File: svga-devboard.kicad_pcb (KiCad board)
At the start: 4 copper layers, 130 x 106.7 mm, 40 parts, among them J1 Bus_PCI_32bit_Universal, U1 SN74LVCH16T245DGGR, U2 SN74LVCH16T245DGGR, U3 SN74LVCH16T245DGGR, U4 SN74LVCH16T245DGGR, U5 SN74LVCH16T245DGGR

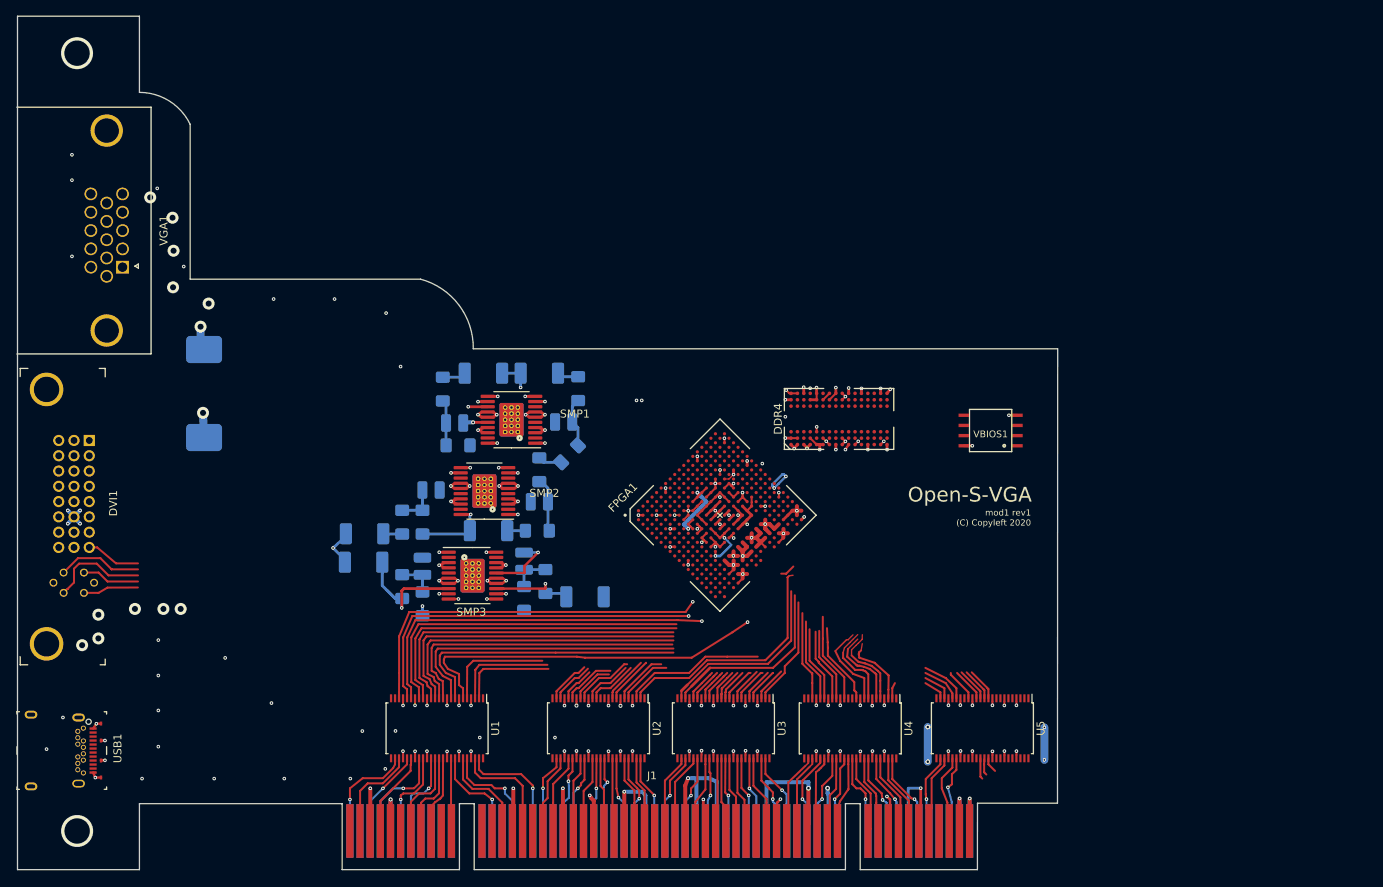
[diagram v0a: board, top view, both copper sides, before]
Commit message: Add files via upload
Converted to hierarchical scheets, added support-components for SMPS-units - many other changes.
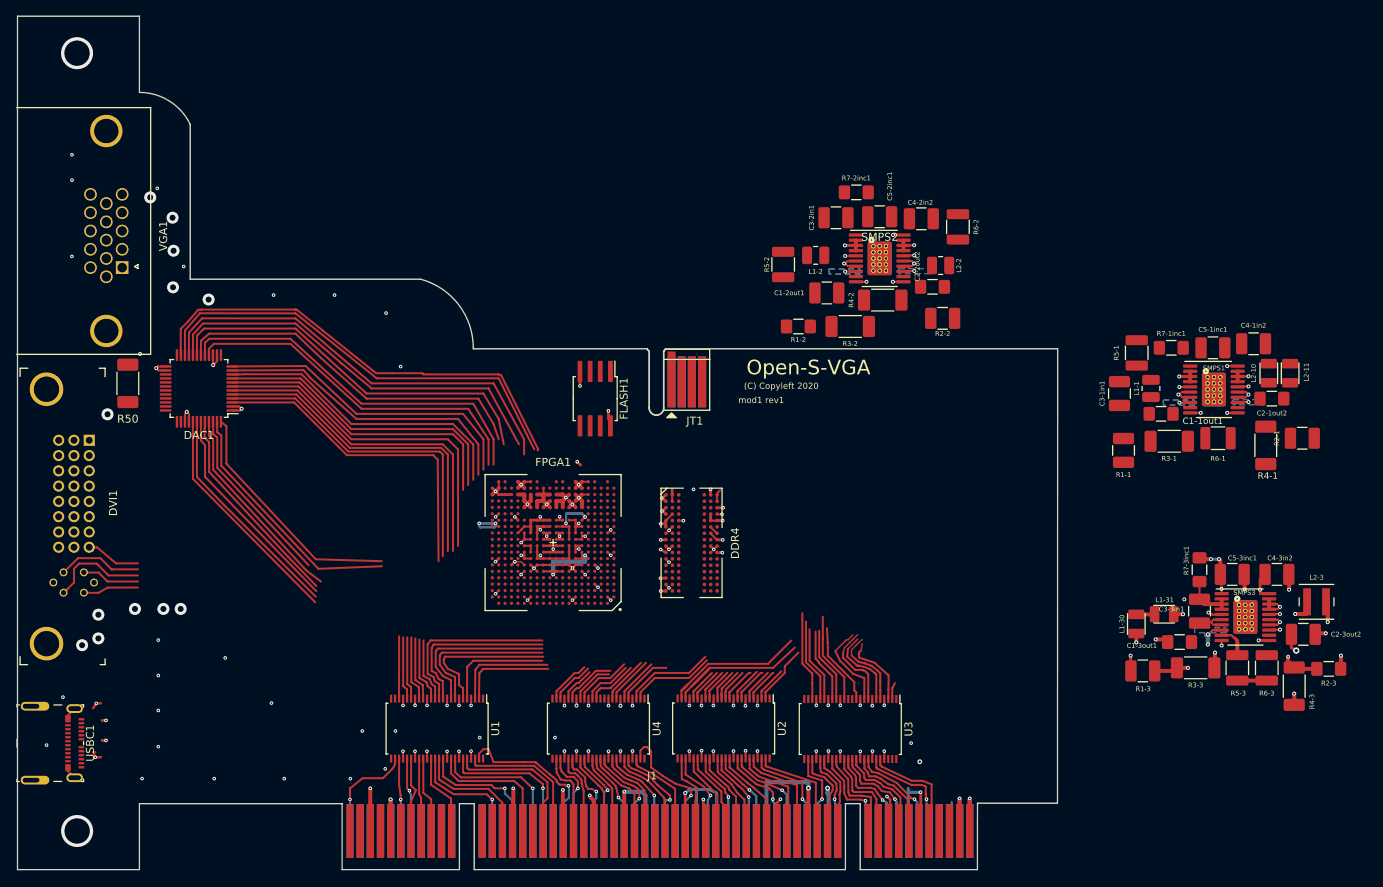
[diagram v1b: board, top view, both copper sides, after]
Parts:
- removed C1-1, C1-2, C1-3, C2-1, C2-2, C2-3: 22UF-1206-16V-10%, Capacitor_SMD:C_1206_3216Metric_Pad1.42x1.75mm_HandSolder
- removed L1-3, L2-1: 1008PS-102KLC, Inductor_SMD:L_1008_2520Metric
- removed SMP1, SMP2, SMP3: LM26420-Q1MHX_NOPB, Package_SO:HTSSOP-20-1EP_4.4x6.5mm_P0.42mm_EP3.2x6.4mm_Mask3.0x4.2mm_ThermalVias
- removed U5: SN74LVCH16T245DGGR, Package_SO:TSSOP-48_6.1x12.5mm_P0.5mm
- removed USB1: USB_C_Amphenol_10133476-10001LF, Connector_USB:USB-C_Female_10133476-10001LF
- removed VBIOS1: Cypress_Semi_S25FL128LAGMFV013, Package_SO:Cypress_Semi_S25FL128LAGMFV013
- added C1-1out1: C3216X7S0J336M160AC, Capacitor_SMD:C_1206_3216Metric_Pad1.42x1.75mm_HandSolder, F.Cu at (221.9, 76.8)
- added C1-2out1: C3225X7R1C226M250AC, Capacitor_SMD:C_1210_3225Metric_Pad1.42x2.65mm_HandSolder, F.Cu at (180.1, 61.7)
- added C1-3out1: C3216X7S0J336M160AC, Capacitor_SMD:C_1206_3216Metric_Pad1.42x1.75mm_HandSolder, F.Cu at (224.2, 105.4)
- added C2-1out2: C3216X7S0J336M160AC, Capacitor_SMD:C_1206_3216Metric_Pad1.42x1.75mm_HandSolder, F.Cu at (235.7, 74.9)
- added C2-2out2: C3216X7S0J336M160AC, Capacitor_SMD:C_1206_3216Metric_Pad1.42x1.75mm_HandSolder, F.Cu at (193.3, 61.0)
- added C2-3out2: C3225X7R1C226M250AC, Capacitor_SMD:C_1210_3225Metric_Pad1.42x2.65mm_HandSolder, F.Cu at (239.6, 104.4)
- added C3-1in1: C1210C156K8PACTU, Capacitor_SMD:C_1210_3225Metric_Pad1.42x2.65mm_HandSolder, F.Cu at (216.7, 74.3)
- added C3-2in1: C1210C156K8PACTU, Capacitor_SMD:C_1210_3225Metric_Pad1.42x2.65mm_HandSolder, F.Cu at (181.2, 52.3)
- added C3-3in1: C1210C156K8PACTU, Capacitor_SMD:C_1210_3225Metric_Pad1.42x2.65mm_HandSolder, F.Cu at (226.7, 101.5)
- added C4-1in2: C1210C156K8PACTU, Capacitor_SMD:C_1210_3225Metric_Pad1.42x2.65mm_HandSolder, F.Cu at (233.4, 68.1)
- added C4-2in2: C1210C156K8PACTU, Capacitor_SMD:C_1210_3225Metric_Pad1.42x2.65mm_HandSolder, F.Cu at (191.9, 52.5)
- added C4-3in2: C1210C156K8PACTU, Capacitor_SMD:C_1210_3225Metric_Pad1.42x2.65mm_HandSolder, F.Cu at (236.3, 96.9)
- added C5-1inc1: C1210C474K5RACTU, Capacitor_SMD:C_1210_3225Metric_Pad1.42x2.65mm_HandSolder, F.Cu at (228.3, 68.6)
- added C5-2inc1: C1210C474K5RACTU, Capacitor_SMD:C_1210_3225Metric_Pad1.42x2.65mm_HandSolder, F.Cu at (186.7, 52.2)
- added C5-3inc1: C1210C474K5RACTU, Capacitor_SMD:C_1210_3225Metric_Pad1.42x2.65mm_HandSolder, F.Cu at (230.8, 96.9)
- added DAC1: ADV7125KSTZ50, Package_QFP:LQFP-48_7x7mm_P0.5mm, F.Cu at (101.6, 73.7)
- added FLASH1: ISSI_IS25LP128F-JBLE, Package_SO:SOIC-8_5.28x5.28mm_P1.27mm, F.Cu at (151.1, 74.9)
- added JT1: JT1, Connector_PCBEdge:con-pcb-slot-CONN_SLOT, F.Cu at (162.6, 72.6)
- added L1-30: MAKK2520HR22M, Inductor_SMD:L_Taiyo-Yuden_MA-2520_HandSoldering, F.Cu at (218.8, 103.1)
- added L1-31: MAKK2520HR33M, Inductor_SMD:L_Taiyo-Yuden_MA-2520_HandSoldering, F.Cu at (222.2, 101.9)
- added L2-10: MAKK2520HR22M, Inductor_SMD:L_Taiyo-Yuden_MA-2520_HandSoldering, F.Cu at (235.3, 71.8)
- added L2-11: MAKK2520HR33M, Inductor_SMD:L_Taiyo-Yuden_MA-2520_HandSoldering, F.Cu at (238.0, 71.8)
- added R5-1: RC1210FR-0749K9L, Resistor_SMD:R_YAGEO_1210_3225Metric_HandSolder, F.Cu at (218.8, 69.2)
- added R5-2: RC1210FR-0749K9L, Resistor_SMD:R_YAGEO_1210_3225Metric_HandSolder, F.Cu at (174.6, 58.2)
- added R5-3: RC1210FR-0749K9L, Resistor_SMD:R_YAGEO_1210_3225Metric_HandSolder, F.Cu at (231.4, 108.6)
- added R6-1: RC1210FR-0749K9L, Resistor_SMD:R_YAGEO_1210_3225Metric_HandSolder, F.Cu at (229.0, 79.9)
- added R6-2: RC1210FR-0749K9L, Resistor_SMD:R_YAGEO_1210_3225Metric_HandSolder, F.Cu at (196.5, 53.5)
- added R6-3: RC1210FR-0749K9L, Resistor_SMD:R_YAGEO_1210_3225Metric_HandSolder, F.Cu at (235.1, 108.6)
- added R7-1inc1: CRCW12064R99FKEAHP, Resistor_SMD:R_1206_3216Metric_Pad1.42x1.75mm_HandSolder, F.Cu at (223.1, 68.6)
- added R7-2inc1: CRCW12064R99FKEAHP, Resistor_SMD:R_1206_3216Metric_Pad1.42x1.75mm_HandSolder, F.Cu at (183.8, 49.1)
- added R7-3inc1: CRCW12064R99FKEAHP, Resistor_SMD:R_1206_3216Metric_Pad1.42x1.75mm_HandSolder, F.Cu at (226.7, 96.3)
- added SMPS1: LM26420-Q1MHX_NOPB, Package_SO:HTSSOP-20-1EP_4.4x6.5mm_P0.42mm_EP3.2x6.4mm_Mask3.0x4.2mm_ThermalVias, F.Cu at (228.5, 73.8)
- added SMPS2: LM26420-Q1MHX_NOPB, Package_SO:HTSSOP-20-1EP_4.4x6.5mm_P0.42mm_EP3.2x6.4mm_Mask3.0x4.2mm_ThermalVias, F.Cu at (186.7, 57.4)
- added SMPS3: LM26420-Q1MHX_NOPB, Package_SO:HTSSOP-20-1EP_4.4x6.5mm_P0.42mm_EP3.2x6.4mm_Mask3.0x4.2mm_ThermalVias, F.Cu at (232.4, 102.2)
- added USBC1: USB_C_Molex_201267-0005, Connector_USB:USB-C_Receptacle_2012670005, F.Cu at (82.9, 118.0)
- FPGA1: value LFE5U-85F-BG381 -> LFE5U-85F-BG381-LRJ
- J1: value Bus_PCI_32bit_Universal -> Bus_PCI_32bit_Universal_lrj
- L1-1, L2-2, R2-3, R3-1, R3-2, R3-3, R4-1, R4-2, R4-3: moved to F.Cu
- L1-2: value 1008PS-102KLC -> 1008PS-152KLC; moved to F.Cu
- L2-3: value 1008PS-102KLC -> XFL4015-701MEC; footprint Inductor_SMD:L_1008_2520Metric -> Inductor_SMD:L_Coilcraft_XFL4015; moved to F.Cu
- R1-1: value CRCW12064R99FKEAHP -> CRCW121012K7FKEA; footprint Resistor_SMD:R_1206_3216Metric_Pad1.42x1.75mm_HandSolder -> Resistor_SMD:R_1210_3225Metric_Pad1.42x2.65mm_HandSolder; moved to F.Cu
- R1-2: value CRCW12064R99FKEAHP -> ERJ-8ENF2152V; moved to F.Cu
- R1-3, R2-1: value CRCW12064R99FKEAHP -> ERJ-14NF3741U; footprint Resistor_SMD:R_1206_3216Metric_Pad1.42x1.75mm_HandSolder -> Resistor_SMD:R_1210_3225Metric_Pad1.42x2.65mm_HandSolder; moved to F.Cu
- R2-2: value CRCW12064R99FKEAHP -> RC1210FR-074K99L; footprint Resistor_SMD:R_1206_3216Metric_Pad1.42x1.75mm_HandSolder -> Resistor_SMD:R_1210_3225Metric_Pad1.42x2.65mm_HandSolder; moved to F.Cu
- R50: value TE_CGS_SMF52M0JT_1MOHM-_5W-5% -> CMP2010-FX-1004ELF; footprint Resistor_SMD:TE_CGS_SMF52M0JT_Pad3.4x4.5mm -> Resistor_SMD:R_2010_5025Metric_Pad1.52x2.65mm_HandSolder; moved to F.Cu
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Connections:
- net +12V renamed Net-(J1-PadA2)
- net -12V renamed Net-(J1-PadB1)
- net /66M renamed /Signal Voltage-level translation/A-22
- net /A-02 renamed /Signal Voltage-level translation/FR_ME
- net /A-03 renamed /Signal Voltage-level translation/CB_2
- net /A-04 renamed /Signal Voltage-level translation/A-17
- net /A-05 renamed /Signal Voltage-level translation/A-16
- net /A-06 renamed /Signal Voltage-level translation/A-18
- net /A-07 renamed /Signal Voltage-level translation/A-19
- net /A-08 renamed /Signal Voltage-level translation/A-20
- net /A-09 renamed /Signal Voltage-level translation/A-23
- net /A-10 renamed /Signal Voltage-level translation/IDSL
- net /A-11 renamed /Signal Voltage-level translation/CBE3_
- net /A-12 renamed /Signal Voltage-level translation/A-24
- net /A-13 renamed /Signal Voltage-level translation/A-25
- net /A-14 renamed /Signal Voltage-level translation/A-26
- net /A-15 renamed Net-(U3-Pad2)
- net /A-16 renamed /Signal Voltage-level translation/A-10
- net /A-17 renamed /Signal Voltage-level translation/A-11
- net /A-18 renamed /Signal Voltage-level translation/A-12
- net /A-19 renamed /Signal Voltage-level translation/A-13
- net /A-20 renamed /Signal Voltage-level translation/A-14
- net /A-21 renamed /Signal Voltage-level translation/CBE1_
- net /A-22 renamed /Signal Voltage-level translation/A-15
- net /A-23 renamed /Signal Voltage-level translation/PAR_
- net /A-24 renamed /Signal Voltage-level translation/SMCLK_
- net /A-25 renamed /Signal Voltage-level translation/PERR_
- net /A-26 renamed /Signal Voltage-level translation/LOCK_
- net /A-27 renamed /Signal Voltage-level translation/STOP_
- net /A-28 renamed /Signal Voltage-level translation/XC_P
- net /A-29 renamed /Signal Voltage-level translation/DEVSL
- net /A-30 renamed /Signal Voltage-level translation/IRD_
- net /A-31 renamed /Signal Voltage-level translation/TRD_
- net /AC64 renamed Net-(J1-PadB60)
- net /CBE0_ renamed /Signal Voltage-level translation/A-21
- net /CB_2 renamed /Signal Voltage-level translation/A-09
- net /DVSL renamed /Signal Voltage-level translation/A-07
- net /FRME renamed /Signal Voltage-level translation/66M
- net /GNT_ renamed /Signal Voltage-level translation/A-31
- net /INTA_ renamed /Signal Voltage-level translation/PRSN_1
- net /INTB_ renamed /Signal Voltage-level translation/RST_
- net /INTC_ renamed /Signal Voltage-level translation/PRSN_2
- net /INTD_ renamed /Signal Voltage-level translation/CLK_
- net /IRD_ renamed /Signal Voltage-level translation/CBE0_
- net /LOC_ renamed /Signal Voltage-level translation/A-05
- net /PAR_ renamed Net-(U3-Pad3)
- net /PER_ renamed /Signal Voltage-level translation/A-03
- net /PME_ renamed /Signal Voltage-level translation/A-28
- net /PRSN_1 renamed /Signal Voltage-level translation/GNT_
- net /PRSN_2 renamed /Signal Voltage-level translation/REQ_
- net /REQ64 renamed Net-(J1-PadA60)
- net /REQ_ renamed /Signal Voltage-level translation/A-29
- net /RST_ renamed /Signal Voltage-level translation/PME_
- net /SCLK renamed /Signal Voltage-level translation/A-02
- net /SDAT renamed /Signal Voltage-level translation/A-1
- net /SER_ renamed /Signal Voltage-level translation/A-0
- net /STO_ renamed /Signal Voltage-level translation/A-04
- net /TRD_ renamed /Signal Voltage-level translation/A-08
- net /TRST_ renamed /Signal Voltage-level translation/TRST_
- net /XCA_ renamed /Signal Voltage-level translation/A-06
- net Net-(DDR4-PadT8) renamed /DRAM/A13_DRAM
- net Net-(FPGA1-PadK3) renamed /DRAM/D4_DRAM
- net Net-(J1-PadA40) renamed /PCI/PCI_SMCLK
- net Net-(J1-PadA41) renamed /PCI/PCI_SMDAT
- net Net-(U2-Pad11) renamed /Signal Voltage-level translation/SERR_
- net Net-(U2-Pad12) renamed /Signal Voltage-level translation/SMDAT_
- net Net-(U4-Pad23) renamed /Signal Voltage-level translation/A-27
- DDR4 pad A1: /2.5V1 -> /DRAM/1.2V
- DDR4 pad A3: Net-(DDR4-PadA3) -> /DRAM/D8_DRAM
- DDR4 pad A9: /1.2V1 -> /DRAM/1.2V
- DDR4 pad B1: /2.5V1 -> /DRAM/2.5V
- DDR4 pad B3: /1.2V1 -> /DRAM/1.2V
- DDR4 pad B8: Net-(DDR4-PadB8) -> /DRAM/D9_DRAM
- DDR4 pad B9: /1.2V1 -> /DRAM/1.2V
- DDR4 pad C1: /1.2V1 -> /DRAM/1.2V
- DDR4 pad C2: Net-(DDR4-PadC2) -> /DRAM/D12_DRAM
- DDR4 pad C3: Net-(DDR4-PadC3) -> /DRAM/D10_DRAM
- DDR4 pad C7: Net-(DDR4-PadC7) -> /DRAM/D11_DRAM
- DDR4 pad C8: Net-(DDR4-PadC8) -> /DRAM/D13_DRAM
- DDR4 pad D1: /1.2V1 -> /DRAM/1.2V
- DDR4 pad D3: Net-(DDR4-PadD3) -> /DRAM/D14_DRAM
- DDR4 pad D7: Net-(DDR4-PadD7) -> /DRAM/D15_DRAM
- DDR4 pad D9: /1.2V1 -> /DRAM/1.2V
- DDR4 pad F2: /1.2V1 -> /DRAM/1.2V
- DDR4 pad F7: Net-(DDR4-PadF7) -> /DRAM/D1_DRAM
- DDR4 pad F8: /1.2V1 -> /DRAM/1.2V
- DDR4 pad G1: /1.2V1 -> /DRAM/1.2V
- DDR4 pad G2: Net-(DDR4-PadG2) -> /DRAM/D0_DRAM
- DDR4 pad G7: /1.2V1 -> /DRAM/1.2V
- DDR4 pad G9: /1.2V1 -> /DRAM/1.2V
- DDR4 pad H2: Net-(DDR4-PadH2) -> /DRAM/D2_DRAM
- DDR4 pad H7: Net-(DDR4-PadH7) -> /DRAM/D3_DRAM
- DDR4 pad H8: Net-(DDR4-PadH8) -> /DRAM/D5_DRAM
- DDR4 pad J1: /1.2V1 -> /DRAM/1.2V
- DDR4 pad J2: /1.2V1 -> /DRAM/1.2V
- DDR4 pad J3: Net-(DDR4-PadJ3) -> /DRAM/D6_DRAM
- DDR4 pad J7: Net-(DDR4-PadJ7) -> /DRAM/D7_DRAM
- DDR4 pad J8: /1.2V1 -> /DRAM/1.2V
- DDR4 pad J9: /1.2V1 -> /DRAM/1.2V
- DDR4 pad K7: Net-(DDR4-PadK7) -> /DRAM/CK_DRAM
- DDR4 pad K8: Net-(DDR4-PadK8) -> /DRAM/C#_DRAM
- DDR4 pad L1: /1.2V1 -> /DRAM/1.2V
- DDR4 pad L2: Net-(DDR4-PadL2) -> /DRAM/WE#_DRAM
- DDR4 pad L7: Net-(DDR4-PadL7) -> /DRAM/CS#_DRAM
- DDR4 pad L8: Net-(DDR4-PadL8) -> /DRAM/RAS_DRAM
- DDR4 pad L9: /1.2V1 -> /DRAM/1.2V
- DDR4 pad N3: Net-(DDR4-PadN3) -> /DRAM/A4_DRAM
- DDR4 pad N7: Net-(DDR4-PadN7) -> /DRAM/A3_DRAM
- DDR4 pad P2: Net-(DDR4-PadP2) -> /DRAM/A6_DRAM
- DDR4 pad P3: Net-(DDR4-PadP3) -> /DRAM/A0_DRAM
- DDR4 pad P7: Net-(DDR4-PadP7) -> /DRAM/A1_DRAM
- DDR4 pad P8: Net-(DDR4-PadP8) -> /DRAM/A5_DRAM
- DDR4 pad R1: /1.2V1 -> /DRAM/1.2V
- DDR4 pad R2: Net-(DDR4-PadR2) -> /DRAM/A8_DRAM
- DDR4 pad R3: Net-(DDR4-PadR3) -> /DRAM/A2_DRAM
- DDR4 pad R7: Net-(DDR4-PadR7) -> /DRAM/A9_DRAM
- DDR4 pad R8: Net-(DDR4-PadR8) -> /DRAM/A7_DRAM
- DDR4 pad R9: /2.5V1 -> /DRAM/2.5V
- DDR4 pad T2: Net-(DDR4-PadT2) -> /DRAM/A11_DRAM
- DDR4 pad T9: /1.2V1 -> /DRAM/1.2V
- DVI1 pad 15: Net-(DVI1-Pad15) -> GND
- DVI1 pad 7: GND -> Net-(DVI1-Pad7)
- DVI1 pad C1: Net-(DVI1-PadC1) -> Net-(DAC1-Pad34)
- DVI1 pad C2: Net-(DVI1-PadC2) -> Net-(DAC1-Pad32)
- DVI1 pad C3: Net-(DVI1-PadC3) -> Net-(DAC1-Pad28)
- DVI1 pad C5: GNDA -> Net-(DVI1-PadC5)
- DVI1 pad SH: GNDA -> Net-(DVI1-PadC5)
- FPGA1 pad A4: Net-(FPGA1-PadA4) -> /DRAM/A7_DRAM
- FPGA1 pad A5: Net-(FPGA1-PadA5) -> /DRAM/A11_DRAM
- FPGA1 pad B1: Net-(FPGA1-PadB1) -> /DRAM/A9_DRAM
- FPGA1 pad B2: /0.8V2 -> /DRAM/0.8V
- FPGA1 pad B4: Net-(FPGA1-PadB4) -> /DRAM/A5_DRAM
- FPGA1 pad C1: Net-(FPGA1-PadC1) -> /DRAM/A2_DRAM
- FPGA1 pad C18: Net-(FPGA1-PadC18) -> /VGA + DVI connectors/RED1
- FPGA1 pad C20: Net-(FPGA1-PadC20) -> /VGA + DVI connectors/RED0
- FPGA1 pad C4: Net-(FPGA1-PadC4) -> /DRAM/A8_DRAM
- FPGA1 pad D1: Net-(FPGA1-PadD1) -> /DRAM/A0_DRAM
- FPGA1 pad D18: Net-(FPGA1-PadD18) -> /VGA + DVI connectors/RED3
- FPGA1 pad D19: Net-(FPGA1-PadD19) -> /VGA + DVI connectors/RED2
- FPGA1 pad D20: /0.8V2 -> /VGA + DVI connectors/0.8V
- FPGA1 pad D5: Net-(FPGA1-PadD5) -> /DRAM/A1_DRAM
- FPGA1 pad E17: Net-(FPGA1-PadE17) -> /VGA + DVI connectors/RED5
- FPGA1 pad E20: Net-(FPGA1-PadE20) -> /VGA + DVI connectors/RED4
- FPGA1 pad E3: Net-(FPGA1-PadE3) -> /DRAM/A3_DRAM
- FPGA1 pad E4: Net-(FPGA1-PadE4) -> /DRAM/RAS_DRAM
- FPGA1 pad F1: Net-(FPGA1-PadF1) -> /DRAM/CS#_DRAM
- FPGA1 pad F10: /2.5V1 -> /Power/2.5V
- FPGA1 pad F11: /2.5V1 -> /Power/2.5V
- FPGA1 pad F12: /2.5V1 -> /Power/2.5V
- FPGA1 pad F15: /1.1V1 -> /Power/2.5V
- FPGA1 pad F17: Net-(FPGA1-PadF17) -> /VGA + DVI connectors/RED6
- FPGA1 pad F3: Net-(FPGA1-PadF3) -> /DRAM/A6_DRAM
- FPGA1 pad F4: Net-(FPGA1-PadF4) -> /DRAM/A4_DRAM
- FPGA1 pad F6: /1.1V1 -> /Power/2.5V
- FPGA1 pad F9: /2.5V1 -> /Power/2.5V
- FPGA1 pad G18: Net-(FPGA1-PadG18) -> /VGA + DVI connectors/RED7
- FPGA1 pad G19: Net-(FPGA1-PadG19) -> /VGA + DVI connectors/GRE0
- FPGA1 pad G2: Net-(FPGA1-PadG2) -> /DRAM/WE#_DRAM
- FPGA1 pad G3: Net-(FPGA1-PadG3) -> /DRAM/C#_DRAM
- FPGA1 pad G5: Net-(FPGA1-PadG5) -> /DRAM/CK_DRAM
- FPGA1 pad H10: /1.1V1 -> /Power/1.1V_1
- FPGA1 pad H11: /1.1V1 -> /Power/1.1V_1
- FPGA1 pad H12: /1.1V1 -> /Power/1.1V_1
- FPGA1 pad H13: /1.1V1 -> /Power/1.1V_1
- FPGA1 pad H14: /2.5V1 -> /Power/2.5V
- FPGA1 pad H15: /2.5V1 -> /Power/2.5V
- FPGA1 pad H17: Net-(FPGA1-PadH17) -> /VGA + DVI connectors/GRE1
- FPGA1 pad H18: Net-(FPGA1-PadH18) -> /VGA + DVI connectors/GRE3
- FPGA1 pad H20: Net-(FPGA1-PadH20) -> /VGA + DVI connectors/GRE2
- FPGA1 pad H4: Net-(FPGA1-PadH4) -> /DRAM/D2_DRAM
- FPGA1 pad H6: /2.5V1 -> /Power/2.5V
- FPGA1 pad H7: /2.5V1 -> /Power/2.5V
- FPGA1 pad H8: /1.1V1 -> /Power/1.1V_1
- FPGA1 pad H9: /1.1V1 -> /Power/1.1V_1
- FPGA1 pad J1: Net-(FPGA1-PadJ1) -> /DRAM/D7_DRAM
- FPGA1 pad J13: /1.1V1 -> /Power/1.1V_1
- FPGA1 pad J15: /2.5V1 -> /Power/2.5V
- FPGA1 pad J19: Net-(FPGA1-PadJ19) -> /VGA + DVI connectors/GRE4
- FPGA1 pad J4: Net-(FPGA1-PadJ4) -> /DRAM/D5_DRAM
- FPGA1 pad J5: Net-(FPGA1-PadJ5) -> /DRAM/D3_DRAM
- FPGA1 pad J6: /2.5V1 -> /Power/2.5V
- FPGA1 pad J8: /1.1V1 -> /Power/1.1V_1
- FPGA1 pad K13: /1.1V1 -> /Power/1.1V_1
- FPGA1 pad K17: Net-(FPGA1-PadK17) -> /VGA + DVI connectors/GRE6
- FPGA1 pad K19: Net-(FPGA1-PadK19) -> /VGA + DVI connectors/GRE5
- FPGA1 pad K2: Net-(FPGA1-PadK2) -> /DRAM/D6_DRAM
- FPGA1 pad K4: Net-(FPGA1-PadK4) -> /DRAM/D1_DRAM
- FPGA1 pad K5: /0.8V2 -> /DRAM/0.8V
- FPGA1 pad K8: /1.1V1 -> /Power/1.1V_1
- FPGA1 pad L13: /1.1V1 -> /Power/1.1V_1
- FPGA1 pad L14: /2.5V1 -> /Power/2.5V
- FPGA1 pad L15: /2.5V1 -> /Power/2.5V
- FPGA1 pad L17: Net-(FPGA1-PadL17) -> /VGA + DVI connectors/SYN
- FPGA1 pad L20: Net-(FPGA1-PadL20) -> /VGA + DVI connectors/GRE7
- FPGA1 pad L6: /2.5V1 -> /Power/2.5V
- FPGA1 pad L7: /2.5V1 -> /Power/2.5V
- FPGA1 pad L8: /1.1V1 -> /Power/1.1V_1
- FPGA1 pad M1: Net-(FPGA1-PadM1) -> /DRAM/D0_DRAM
- FPGA1 pad M13: /1.1V1 -> /Power/1.1V_1
- FPGA1 pad M15: /2.5V1 -> /Power/2.5V
- FPGA1 pad M17: Net-(FPGA1-PadM17) -> /VGA + DVI connectors/BLAN
- FPGA1 pad M20: Net-(FPGA1-PadM20) -> /VGA + DVI connectors/BLU0
- FPGA1 pad M3: Net-(FPGA1-PadM3) -> /DRAM/D15_DRAM
- FPGA1 pad M4: Net-(FPGA1-PadM4) -> /DRAM/D13_DRAM
- FPGA1 pad M5: Net-(FPGA1-PadM5) -> /DRAM/D14_DRAM
- FPGA1 pad M6: /2.5V1 -> /Power/2.5V
- FPGA1 pad M8: /1.1V1 -> /Power/1.1V_1
- FPGA1 pad N10: /1.1V1 -> /Power/1.1V_1
- FPGA1 pad N11: /1.1V1 -> /Power/1.1V_1
- FPGA1 pad N12: /1.1V1 -> /Power/1.1V_1
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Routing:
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- added copper zone on B.Cu, net (none)
- added copper zone on Power, net /Power/0.8V
- added copper zone on Power, net /Power/1.1V_2
- added copper zone on Power, net Net-(C5-3inc1-Pad1)
- added copper zone on Power, net Net-(L1-31-Pad2)
- added copper zone on Power, net Net-(L2-3-Pad1)
- added copper zone on B.Cu, net Net-(R1-3-Pad2)
- added copper zone on Power, net Net-(R2-3-Pad1)
- removed copper zone on Power, net /0.8V2
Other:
- outline, holes or cut-outs redrawn

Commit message: Add files via upload
Added Pull-up and pull-down resistors for JTAG and sysConfig connections.
Added pinheaders for FPGA-Configuration. (replacing edge-connector)
Combined the DVI+VGA and USB-C hierarchical sheets into one.
Assigned a dedicated sheet for the DAC.
Added 75 Ohm terminal-resistors to output of DAC.
Placed filtering-capacitors for DAC VAA.
Connected VGA ID-bits and DVI DDC together.
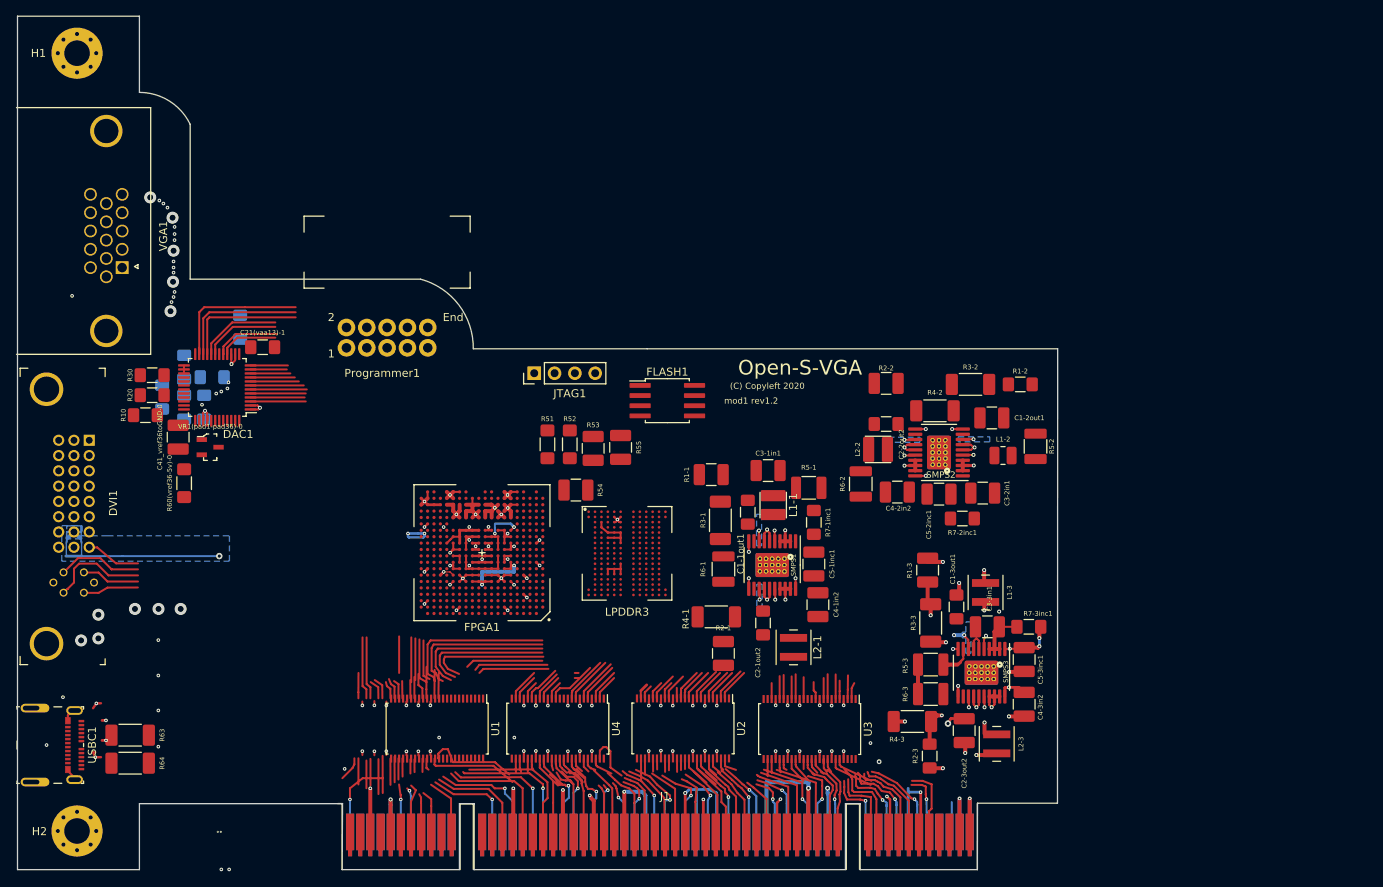
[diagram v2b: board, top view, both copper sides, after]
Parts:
- removed DDR4: AS4C256M16D4-75BCN, Package_BGA:FBGA-96-Alliance_
- removed JT1: JT1, Connector_PCBEdge:con-pcb-slot-CONN_SLOT
- removed L1-30, L2-10: MAKK2520HR22M, Inductor_SMD:L_Taiyo-Yuden_MA-2520_HandSoldering
- removed L1-31, L2-11: MAKK2520HR33M, Inductor_SMD:L_Taiyo-Yuden_MA-2520_HandSoldering
- removed R50: CMP2010-FX-1004ELF, Resistor_SMD:R_2010_5025Metric_Pad1.52x2.65mm_HandSolder
- added C10(vaa29)-0: VJ1206Y104JXAAR, Capacitor_SMD:C_1206_3216Metric_Pad1.42x1.75mm_HandSolder, B.Cu at (97.0, 74.7)
- added C11(vaa29)-1: VJ1206Y103JXAMC, Capacitor_SMD:C_1206_3216Metric_Pad1.42x1.75mm_HandSolder, B.Cu at (103.2, 72.2)
- added C20(vaa13)-0: VJ1206Y104JXAAR, Capacitor_SMD:C_1206_3216Metric_Pad1.42x1.75mm_HandSolder, B.Cu at (106.8, 66.0)
- added C21(vaa13)-1: VJ1206Y103JXAMC, Capacitor_SMD:C_1206_3216Metric_Pad1.42x1.75mm_HandSolder, F.Cu at (109.6, 68.5)
- added C30(vaa30)-0: VJ1206Y104JXAAR, Capacitor_SMD:C_1206_3216Metric_Pad1.42x1.75mm_HandSolder, B.Cu at (99.8, 76.0)
- added C31(vaa30)-1: VJ1206Y103JXAMC, Capacitor_SMD:C_1206_3216Metric_Pad1.42x1.75mm_HandSolder, B.Cu at (99.8, 71.0)
- added C41_vref36toGND-0: C1210C156K8PACTU, Capacitor_SMD:C_1210_3225Metric_Pad1.42x2.65mm_HandSolder, F.Cu at (99.0, 79.8)
- added C42(+5to35)1: VJ1206Y104JXAAR, Capacitor_SMD:C_1206_3216Metric_Pad1.42x1.75mm_HandSolder, B.Cu at (102.2, 76.0)
- added H1: MountingHole_Pad, MountingHole:MountingHole_3.2mm_M3_Pad_Via, F.Cu at (86.4, 31.8)
- added H2: MountingHole_Pad, MountingHole:MountingHole_3.2mm_M3_Pad_Via, F.Cu at (86.4, 129.0)
- added JTAG1: CONN_04JST-PTH, Connector_PinHeader_2.54mm:PinHeader_1x04_P2.54mm_Vertical, F.Cu at (143.5, 71.8)
- added L1-3: XFL4015-701MEC, Inductor_SMD:L_Coilcraft_XFL4015, F.Cu at (199.9, 99.2)
- added L2-1: XFL4015-701MEC, Inductor_SMD:L_Coilcraft_XFL4015, F.Cu at (175.9, 106.0)
- added LPDDR3: W63CH2MBVACE, Package_BGA:Winbond_VFBGA-178_W63CH2MBVACE, F.Cu at (155.1, 94.3)
- added Programmer1: Wurth_WR-BHD_61201021721, Connector_PinHeader_2.54mm:WE_WR-BHD_RA_2x5_P2.54mm_Drill1.2mm, F.Cu at (125.1, 67.3)
- added R10: CRCW120675R0FKEA, Resistor_SMD:R_1206_3216Metric_Pad1.42x1.75mm_HandSolder, F.Cu at (94.9, 77.0)
- added R20: CRCW120675R0FKEA, Resistor_SMD:R_1206_3216Metric_Pad1.42x1.75mm_HandSolder, F.Cu at (95.8, 74.5)
- added R30: CRCW120675R0FKEA, Resistor_SMD:R_1206_3216Metric_Pad1.42x1.75mm_HandSolder, F.Cu at (95.8, 72.0)
- added R51: ERJ-8ENF4701V, Resistor_SMD:R_Panasonic_1206_3216Metric_ERJ8EN_HandSolder, F.Cu at (145.2, 80.6)
- added R52: ERJ-8ENF4701V, Resistor_SMD:R_Panasonic_1206_3216Metric_ERJ8EN_HandSolder, F.Cu at (148.0, 80.6)
- added R53: ERJ-14YJ103U, Resistor_SMD:R_1210_3225Metric_Pad1.42x2.65mm_HandSolder, F.Cu at (150.9, 81.2)
- added R54: RC1210FR-071KL, Resistor_SMD:R_1210_3225Metric_Pad1.42x2.65mm_HandSolder, F.Cu at (148.7, 86.4)
- added R55: ERJ-14YJ103U, Resistor_SMD:R_1210_3225Metric_Pad1.42x2.65mm_HandSolder, F.Cu at (154.3, 81.0)
- added R60(vref36-5v)-0: ERJ-8ENF1001V, Resistor_SMD:R_Panasonic_1206_3216Metric_ERJ8EN_HandSolder, F.Cu at (99.8, 85.5)
- added R63: CMP2010-FX-1004ELF, Resistor_SMD:R_2010_5025Metric_Pad1.52x2.65mm_HandSolder, F.Cu at (93.0, 117.0)
- added R64: CMP2010-FX-1004ELF, Resistor_SMD:R_2010_5025Metric_Pad1.52x2.65mm_HandSolder, F.Cu at (93.0, 120.5)
- added VR1(pad1-pad36)-0: AD1580ARTZ-REEL7, digikey-footprints:SOT-23-3, F.Cu at (103.0, 81.0)
- FLASH1: value ISSI_IS25LP128F-JBLE -> ISSI_IS25WP128F-JBLE
- J1: footprint Connector_PCBEdge:BUS_PCI_UNI_32-lrj -> Connector_PCBEdge:BUS_PCI_UNI_32-lrj2
- L1-1, L2-2: value 1008PS-102KLC -> VLS3015CX-1R5M-1; footprint Inductor_SMD:L_1008_2520Metric -> Inductor_SMD:L_TDK_VLS3015CX-1_handsoldering
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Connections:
- net /PCI/PCI_M66 renamed /PCI/PCI_M66EN
- net /Power/1.2V renamed +1V2
- net /Signal Voltage-level translation/66M renamed /Signal Voltage-level translation/M66EN_VT
- net /Signal Voltage-level translation/A-0 renamed /Signal Voltage-level translation/AD1_VT
- net /Signal Voltage-level translation/A-02 renamed /Signal Voltage-level translation/AD2_VT
- net /Signal Voltage-level translation/A-03 renamed /Signal Voltage-level translation/AD3_VT
- net /Signal Voltage-level translation/A-04 renamed /Signal Voltage-level translation/AD4_VT
- net /Signal Voltage-level translation/A-05 renamed /Signal Voltage-level translation/AD5_VT
- net /Signal Voltage-level translation/A-06 renamed /Signal Voltage-level translation/AD6_VT
- net /Signal Voltage-level translation/A-07 renamed /Signal Voltage-level translation/AD7_VT
- net /Signal Voltage-level translation/A-08 renamed /Signal Voltage-level translation/AD8_VT
- net /Signal Voltage-level translation/A-09 renamed /Signal Voltage-level translation/AD9_VT
- net /Signal Voltage-level translation/A-1 renamed /Signal Voltage-level translation/AD0_VT
- net /Signal Voltage-level translation/A-10 renamed /Signal Voltage-level translation/AD10_VT
- net /Signal Voltage-level translation/A-11 renamed /Signal Voltage-level translation/AD11_VT
- net /Signal Voltage-level translation/A-12 renamed /Signal Voltage-level translation/AD12_VT
- net /Signal Voltage-level translation/A-13 renamed /Signal Voltage-level translation/AD13_VT
- net /Signal Voltage-level translation/A-14 renamed /Signal Voltage-level translation/AD14_VT
- net /Signal Voltage-level translation/A-15 renamed /Signal Voltage-level translation/AD15_VT
- net /Signal Voltage-level translation/A-16 renamed /Signal Voltage-level translation/AD16_VT
- net /Signal Voltage-level translation/A-17 renamed /Signal Voltage-level translation/AD17_VT
- net /Signal Voltage-level translation/A-18 renamed /Signal Voltage-level translation/AD18_VT
- net /Signal Voltage-level translation/A-19 renamed /Signal Voltage-level translation/AD19_VT
- net /Signal Voltage-level translation/A-20 renamed /Signal Voltage-level translation/AD20_VT
- net /Signal Voltage-level translation/A-21 renamed /Signal Voltage-level translation/AD21_VT
- net /Signal Voltage-level translation/A-22 renamed /Signal Voltage-level translation/AD22_VT
- net /Signal Voltage-level translation/A-23 renamed /Signal Voltage-level translation/AD23_VT
- net /Signal Voltage-level translation/A-24 renamed /Signal Voltage-level translation/AD24_VT
- net /Signal Voltage-level translation/A-25 renamed /Signal Voltage-level translation/AD25_VT
- net /Signal Voltage-level translation/A-26 renamed /Signal Voltage-level translation/AD26_VT
- net /Signal Voltage-level translation/A-27 renamed /Signal Voltage-level translation/AD27_VT
- net /Signal Voltage-level translation/A-28 renamed /Signal Voltage-level translation/AD28_VT
- net /Signal Voltage-level translation/A-29 renamed /Signal Voltage-level translation/AD29_VT
- net /Signal Voltage-level translation/A-30 renamed /Signal Voltage-level translation/AD30_VT
- net /Signal Voltage-level translation/A-31 renamed /Signal Voltage-level translation/AD31_VT
- net /Signal Voltage-level translation/CBE0_ renamed /Signal Voltage-level translation/CBE0_VT
- net /Signal Voltage-level translation/CBE1_ renamed /Signal Voltage-level translation/CBE1_VT
- net /Signal Voltage-level translation/CBE3_ renamed /Signal Voltage-level translation/CBE3_VT
- net /Signal Voltage-level translation/CB_2 renamed /Signal Voltage-level translation/CBE2_VT
- net /Signal Voltage-level translation/CLK_ renamed /Signal Voltage-level translation/CLK_VT
- net /Signal Voltage-level translation/DEVSL renamed /Signal Voltage-level translation/DEVSEL_VT
- net /Signal Voltage-level translation/FR_ME renamed /Signal Voltage-level translation/FRAME_VT
- net /Signal Voltage-level translation/GNT_ renamed /Signal Voltage-level translation/GNT_VT
- net /Signal Voltage-level translation/IDSL renamed /Signal Voltage-level translation/IDSEL_VT
- net /Signal Voltage-level translation/INTA_ renamed /Signal Voltage-level translation/INTA_VT
- net /Signal Voltage-level translation/INTB_ renamed /Signal Voltage-level translation/INTB_VT
- net /Signal Voltage-level translation/INTC_ renamed /Signal Voltage-level translation/INTC_VT
- net /Signal Voltage-level translation/INTD_ renamed /Signal Voltage-level translation/INTD_VT
- net /Signal Voltage-level translation/IRD_ renamed /Signal Voltage-level translation/IRDY_VT
- net /Signal Voltage-level translation/LOCK_ renamed /Signal Voltage-level translation/LOCK_VT
- net /Signal Voltage-level translation/M66E renamed /Signal Voltage-level translation/M66EN
- net /Signal Voltage-level translation/PAR_ renamed /Signal Voltage-level translation/PAR_VT
- net /Signal Voltage-level translation/PERR_ renamed /Signal Voltage-level translation/PERR_VT
- net /Signal Voltage-level translation/PME_ renamed /Signal Voltage-level translation/PME_VT
- net /Signal Voltage-level translation/PRSN_1 renamed /Signal Voltage-level translation/PRSNT1_VT
- net /Signal Voltage-level translation/PRSN_2 renamed /Signal Voltage-level translation/PRSNT2_VT
- net /Signal Voltage-level translation/REQ_ renamed /Signal Voltage-level translation/REQ_VT
- net /Signal Voltage-level translation/RST_ renamed /Signal Voltage-level translation/RST_VT
- net /Signal Voltage-level translation/SERR_ renamed /Signal Voltage-level translation/SERR_VT
- net /Signal Voltage-level translation/SMCLK_ renamed /Signal Voltage-level translation/SMCLK_VT
- net /Signal Voltage-level translation/SMDAT_ renamed /Signal Voltage-level translation/SMDAT_VT
- net /Signal Voltage-level translation/STOP_ renamed /Signal Voltage-level translation/STOP_VT
- net /Signal Voltage-level translation/TRD_ renamed /Signal Voltage-level translation/TRDY_VT
- net /Signal Voltage-level translation/TRST_ renamed /Signal Voltage-level translation/TRST_VT
- net /Signal Voltage-level translation/XC_P renamed /Signal Voltage-level translation/XCAP_VT
- net Net-(DVI1-Pad23) renamed /VGA + DVI + USBC/TMDS_CK+
- net Net-(DVI1-Pad24) renamed /VGA + DVI + USBC/TMDS_CK-
- net Net-(FLASH1-Pad3) renamed /JTAG+Config/IO2_FPGA
- net Net-(FLASH1-Pad7) renamed /JTAG+Config/IO3_FPGA
- net Net-(FPGA1-PadA10) renamed /FPGA GPU/AD23_VT
- net Net-(FPGA1-PadA11) renamed /FPGA GPU/AD24_VT
- net Net-(FPGA1-PadA12) renamed /FPGA GPU/LOCK_VT
- net Net-(FPGA1-PadA13) renamed /FPGA GPU/IRDY_VT
- net Net-(FPGA1-PadA14) renamed /FPGA GPU/CBE1_VT
- net Net-(FPGA1-PadA15) renamed /FPGA GPU/AD30_VT
- net Net-(FPGA1-PadA17) renamed /FPGA GPU/GNT_VT
- net Net-(FPGA1-PadA18) renamed /FPGA GPU/PME_VT
- net Net-(FPGA1-PadA19) renamed /FPGA GPU/IDSEL_VT
- net Net-(FPGA1-PadA2) renamed /DRAM/DIR_3B
- net Net-(FPGA1-PadA6) renamed /FPGA GPU/AD14_VT
- net Net-(FPGA1-PadA7) renamed /FPGA GPU/AD10_VT
- net Net-(FPGA1-PadA8) renamed /FPGA GPU/AD11_VT
- net Net-(FPGA1-PadA9) renamed /FPGA GPU/AD21_VT
- net Net-(FPGA1-PadB10) renamed /FPGA GPU/AD22_VT
- net Net-(FPGA1-PadB11) renamed /FPGA GPU/AD25_VT
- net Net-(FPGA1-PadB12) renamed /FPGA GPU/INTB_VT
- net Net-(FPGA1-PadB13) renamed /FPGA GPU/TRDY_VT
- net Net-(FPGA1-PadB15) renamed /FPGA GPU/AD31_VT
- net Net-(FPGA1-PadB16) renamed /FPGA GPU/FRAME_VT
- net Net-(FPGA1-PadB17) renamed /FPGA GPU/SERR_VT
- net Net-(FPGA1-PadB18) renamed /FPGA GPU/REQ_VT
- net Net-(FPGA1-PadB19) renamed /FPGA GPU/CBE3_VT
- net Net-(FPGA1-PadB20) renamed /FPGA GPU/TRST_VT
- net Net-(FPGA1-PadB6) renamed /FPGA GPU/AD15_VT
- net Net-(FPGA1-PadB8) renamed /FPGA GPU/AD9_VT
- net Net-(FPGA1-PadB9) renamed /FPGA GPU/AD19_VT
- net Net-(FPGA1-PadC10) renamed /FPGA GPU/AD20_VT
- net Net-(FPGA1-PadC11) renamed /FPGA GPU/AD26_VT
- net Net-(FPGA1-PadC12) renamed /FPGA GPU/INTD_VT
- net Net-(FPGA1-PadC13) renamed /FPGA GPU/DEVSEL_VT
- net Net-(FPGA1-PadC14) renamed /FPGA GPU/PERR_VT
- net Net-(FPGA1-PadC15) renamed /FPGA GPU/AD29_VT
- net Net-(FPGA1-PadC16) renamed /FPGA GPU/CBE2_VT
- net Net-(FPGA1-PadC17) renamed /FPGA GPU/STOP_VT
- net Net-(FPGA1-PadC6) renamed /FPGA GPU/AD4_VT
- net Net-(FPGA1-PadC7) renamed /FPGA GPU/AD5_VT
- net Net-(FPGA1-PadC8) renamed /FPGA GPU/AD8_VT
- net Net-(FPGA1-PadC9) renamed /FPGA GPU/AD16_VT
- net Net-(FPGA1-PadD10) renamed /FPGA GPU/AD17_VT
- net Net-(FPGA1-PadD11) renamed /FPGA GPU/INTA_VT
- net Net-(FPGA1-PadD12) renamed /FPGA GPU/PRSNT1_VT
- net Net-(FPGA1-PadD13) renamed /FPGA GPU/XCAP_VT
- net Net-(FPGA1-PadD15) renamed /FPGA GPU/AD28_VT
- net Net-(FPGA1-PadD16) renamed /FPGA GPU/CBE0_VT
- net Net-(FPGA1-PadD17) renamed /DAC/CC2_DP
- net Net-(FPGA1-PadD6) renamed /FPGA GPU/AD1_VT
- net Net-(FPGA1-PadD7) renamed /FPGA GPU/AD3_VT
- net Net-(FPGA1-PadD8) renamed /FPGA GPU/AD7_VT
- net Net-(FPGA1-PadD9) renamed /FPGA GPU/AD13_VT
- net Net-(FPGA1-PadE10) renamed /FPGA GPU/AD18_VT
- net Net-(FPGA1-PadE11) renamed /FPGA GPU/INTC_VT
- net Net-(FPGA1-PadE12) renamed /FPGA GPU/PRSNT2_VT
- net Net-(FPGA1-PadE13) renamed /FPGA GPU/PAR_VT
- net Net-(FPGA1-PadE14) renamed /FPGA GPU/SMDAT_VT
- net Net-(FPGA1-PadE19) renamed /DAC/ID_Bit0
- net Net-(FPGA1-PadE6) renamed /FPGA GPU/AD0_VT
- net Net-(FPGA1-PadE7) renamed /FPGA GPU/AD2_VT
- net Net-(FPGA1-PadE8) renamed /FPGA GPU/AD6_VT
- net Net-(FPGA1-PadE9) renamed /FPGA GPU/AD12_VT
- net Net-(FPGA1-PadF19) renamed /DAC/RST_VT
- net Net-(FPGA1-PadG20) renamed /DAC/ID_Bit2
- net Net-(FPGA1-PadK16) renamed /DAC/DDC-C_ID3
- net Net-(FPGA1-PadL16) renamed /DAC/TMDS_CK-
- net Net-(FPGA1-PadN19) renamed /DAC/Hsync_A
- net Net-(U1-Pad1) renamed /Signal Voltage-level translation/DIR_1A
- net Net-(U1-Pad24) renamed /Signal Voltage-level translation/DIR_1B
- net Net-(U1-Pad25) renamed /Signal Voltage-level translation/OE_1B
- net Net-(U1-Pad48) renamed /Signal Voltage-level translation/OE_1A
- net Net-(U2-Pad1) renamed /Signal Voltage-level translation/DIR_2A
- net Net-(U2-Pad24) renamed /Signal Voltage-level translation/DIR_2B
- net Net-(U2-Pad25) renamed /Signal Voltage-level translation/OE_2B
- net Net-(U2-Pad48) renamed /Signal Voltage-level translation/OE_2A
- net Net-(U3-Pad1) renamed /Signal Voltage-level translation/DIR_3A
- net Net-(U3-Pad24) renamed /Signal Voltage-level translation/DIR_3B
- net Net-(U3-Pad25) renamed /Signal Voltage-level translation/OE_3B
- net Net-(U3-Pad48) renamed /Signal Voltage-level translation/OE_3A
- net Net-(U4-Pad1) renamed /Signal Voltage-level translation/DIR_4A
- net Net-(U4-Pad24) renamed /Signal Voltage-level translation/DIR_4B
- net Net-(U4-Pad25) renamed /Signal Voltage-level translation/OE_4B
- net Net-(U4-Pad48) renamed /Signal Voltage-level translation/OE_4A
- net Net-(USBC1-PadA5) renamed /VGA + DVI + USBC/CC1_DP
- net Net-(USBC1-PadB2) renamed /VGA + DVI + USBC/ML_Lane0+
- net Net-(USBC1-PadB3) renamed /VGA + DVI + USBC/ML_Lane0-
- net Net-(USBC1-PadB5) renamed /VGA + DVI + USBC/CC2_DP
- net Net-(VGA1-Pad11) renamed /VGA + DVI + USBC/ID_Bit0
- net Net-(VGA1-Pad4) renamed /VGA + DVI + USBC/ID_Bit2
- C1-1out1 pad 1: /Power/1.8V -> +1V8
- C1-2out1 pad 1: /Power/2.5V -> +2V5
- C1-3out1 pad 1: /Power/1.1V_2 -> +1V1
- C2-1out2 pad 1: /Power/1.1V_1 -> +1V1
- C2-3out2 pad 1: /Power/0.8V -> +0V8
- DAC1 pad 10: /VGA + DVI connectors/GRE7 -> /DAC/GREEN7
- DAC1 pad 11: /VGA + DVI connectors/SYN -> /DAC/BLANK_DAC
- DAC1 pad 12: /VGA + DVI connectors/BLAN -> /DAC/SYNC_DAC
- DAC1 pad 13: +3.3VDAC -> +5V
- DAC1 pad 16: /VGA + DVI connectors/BLU0 -> /DAC/BLUE0
- DAC1 pad 17: /VGA + DVI connectors/BLU1 -> /DAC/BLUE1
- DAC1 pad 18: /VGA + DVI connectors/BLU2 -> /DAC/BLUE2
- DAC1 pad 19: /VGA + DVI connectors/BLU3 -> /DAC/BLUE3
- DAC1 pad 20: /VGA + DVI connectors/BLU4 -> /DAC/BLUE4
- DAC1 pad 21: /VGA + DVI connectors/BLU5 -> /DAC/BLUE5
- DAC1 pad 22: /VGA + DVI connectors/BLU6 -> /DAC/BLUE6
- DAC1 pad 23: /VGA + DVI connectors/BLU7 -> /DAC/BLUE7
- DAC1 pad 24: Net-(DAC1-Pad24) -> /DAC/CLK_DAC
- DAC1 pad 28: Net-(DAC1-Pad28) -> /DAC/ABLUE
- DAC1 pad 29: +3.3VDAC -> +5V
- DAC1 pad 3: /VGA + DVI connectors/GRE0 -> /DAC/GREEN0
- DAC1 pad 30: +3.3VDAC -> +5V
- DAC1 pad 32: Net-(DAC1-Pad32) -> /DAC/AGREEN
- DAC1 pad 34: Net-(DAC1-Pad34) -> /DAC/ARED
- DAC1 pad 4: /VGA + DVI connectors/GRE1 -> /DAC/GREEN1
- DAC1 pad 41: /VGA + DVI connectors/RED0 -> /DAC/RED0
- DAC1 pad 42: /VGA + DVI connectors/RED1 -> /DAC/RED1
- DAC1 pad 43: /VGA + DVI connectors/RED2 -> /DAC/RED2
- DAC1 pad 44: /VGA + DVI connectors/RED3 -> /DAC/RED3
- DAC1 pad 45: /VGA + DVI connectors/RED4 -> /DAC/RED4
- DAC1 pad 46: /VGA + DVI connectors/RED5 -> /DAC/RED5
- DAC1 pad 47: /VGA + DVI connectors/RED6 -> /DAC/RED6
- DAC1 pad 48: /VGA + DVI connectors/RED7 -> /DAC/RED7
- DAC1 pad 5: /VGA + DVI connectors/GRE2 -> /DAC/GREEN2
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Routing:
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- added copper zone on Power, net +1V2
- added copper zone on B.Cu, net GND
- added copper zone on Power, net Net-(L1-31-Pad2)
- removed copper zone on Power, net Net-(L1-3-Pad2)
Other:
- outline, holes or cut-outs redrawn
- board text added: "Minimum BGA-pad size and pad distance"
- board text added: "Minimum Via hole size and hole distance"
- board text added: "mod1 rev1.2"
- board text removed: "mod1 rev1"
